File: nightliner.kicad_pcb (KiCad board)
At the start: 2 copper layers, 154.9 x 116.1 mm, 92 parts, among them J1 TYPE-C-31-M-12, J2 Battery, SW1 pinky_top, SW10 inner_home, SW11 pinky_bottom, SW12 ring_bottom, SW13 middle_bottom, SW14 index_bottom, SW15 inner_bottom, SW16 outer_top, SW17 outer_home, SW18 near_thumb, SW19 home_thumb, SW2 ring_top, SW20 far_thumb, SW21 ON_OFF, SW22 RESET, SW3 middle_top, SW4 index_top, SW5 inner_top, SW6 pinky_home, SW7 ring_home, SW8 middle_home, SW9 index_home, U1 holyiot-18010, U2 TVS2200DRV, U3 USBLC6-2SC6, U4 BQ24075RGT, U5 XC6220B331MR

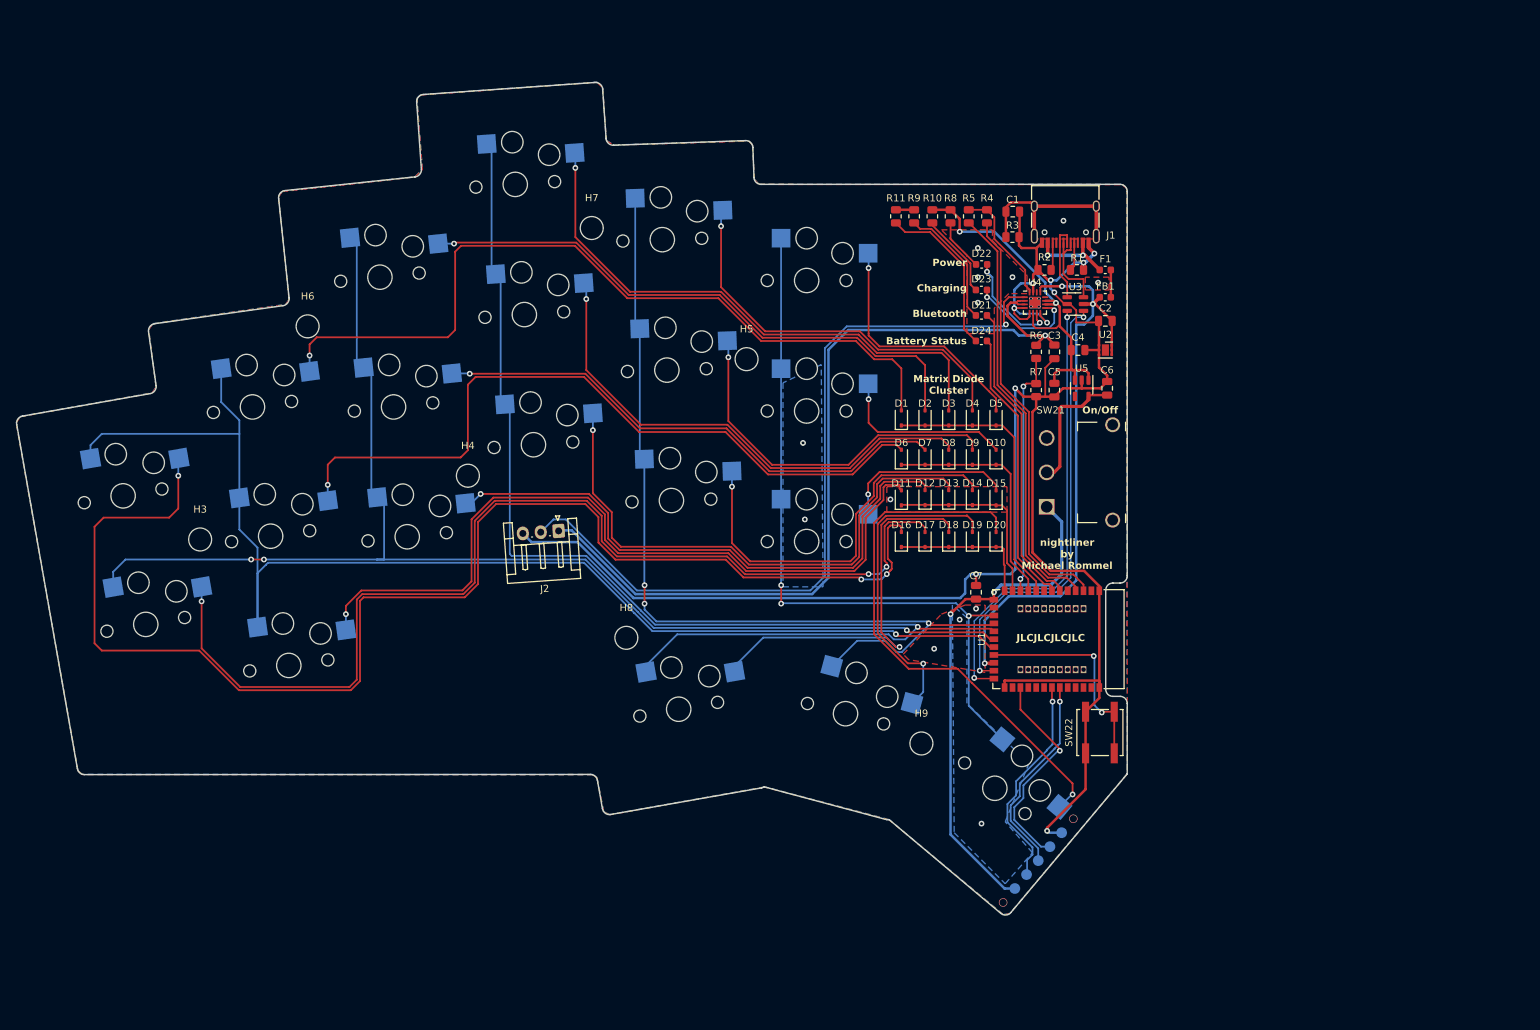
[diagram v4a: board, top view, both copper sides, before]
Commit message: feat: change connector and on/off switch, re-layout
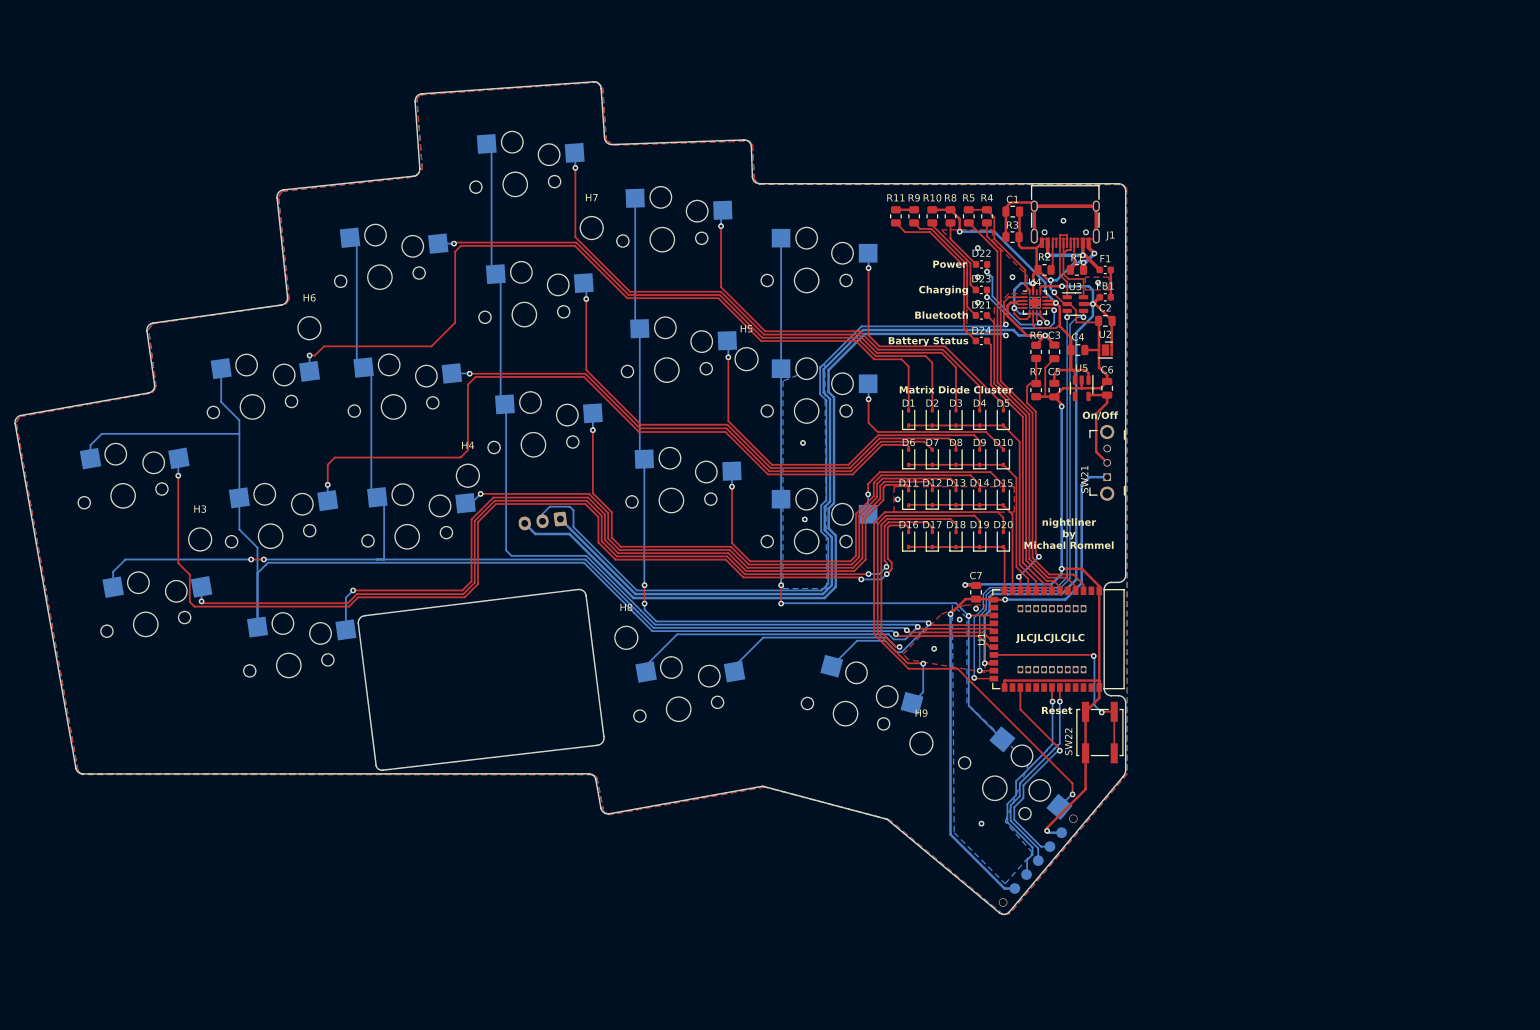
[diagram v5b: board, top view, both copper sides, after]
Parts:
- J2: footprint Connector_JST:JST_EH_S3B-EH_1x03_P2.50mm_Horizontal -> Connector_JST:JST_XH_S3B-XH-A-1_1x03_P2.50mm_Horizontal; moved to B.Cu
- SW21: footprint miro_keyboard:SW_XKB_SS-12D11_SPDT_Angled -> miro_keyboard:SW_ROCPU_SK-12D07-5_SPDT_Angled
- moved SW21 9.40 mm to (170.9, 78.4)
- moved J2 1.67 mm to (94.7, 84.3), turned to -173 degrees
- moved D13 1.02 mm to (149.9, 81.3)
- moved D14 1.02 mm to (153.2, 81.3)
- moved D18 1.02 mm to (149.9, 87.1)
- moved D19 1.02 mm to (153.2, 87.1)
- moved D3 1.02 mm to (149.9, 70.2)
- moved D4 1.02 mm to (153.2, 70.2)
- moved D8 1.02 mm to (149.9, 75.7)
- moved D9 1.02 mm to (153.2, 75.7)
- moved D1 1.02 mm to (143.3, 70.2)
- moved D10 1.02 mm to (156.5, 75.7)
- moved D11 1.02 mm to (143.3, 81.3)
- moved D12 1.02 mm to (146.6, 81.3)
- moved D15 1.02 mm to (156.5, 81.3)
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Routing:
- net Net-(D16-A): track 188.1 -> 146.7 mm
- net Net-(D17-A): track 148.0 -> 129.0 mm
- net GND: track 281.4 -> 296.3 mm, vias 23 -> 25
- net VDD: track 71.5 -> 80.7 mm
- net Net-(SW21-B): track 18.1 -> 13.4 mm
- net /BAT_TEMP: track 110.1 -> 113.9 mm
- net Net-(D11-A): track 108.5 -> 110.2 mm
- net D+: track 63.2 -> 64.8 mm
- net D-: track 63.1 -> 64.5 mm
- net VSENSE: track 34.1 -> 35.4 mm
- net Net-(D6-A): track 103.1 -> 104.3 mm
- net Net-(D2-A): track 81.3 -> 82.5 mm
- net Net-(D13-A): track 77.6 -> 78.6 mm
- net Net-(D9-A): track 51.1 -> 52.1 mm
- net Net-(D8-A): track 71.2 -> 72.2 mm
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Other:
- outline, holes or cut-outs redrawn
- board text added: "LiPo Battery (30mm x 20mm)"
- board text added: "Reset"

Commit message: fix: footprint for prog header, mounting holes, drc check
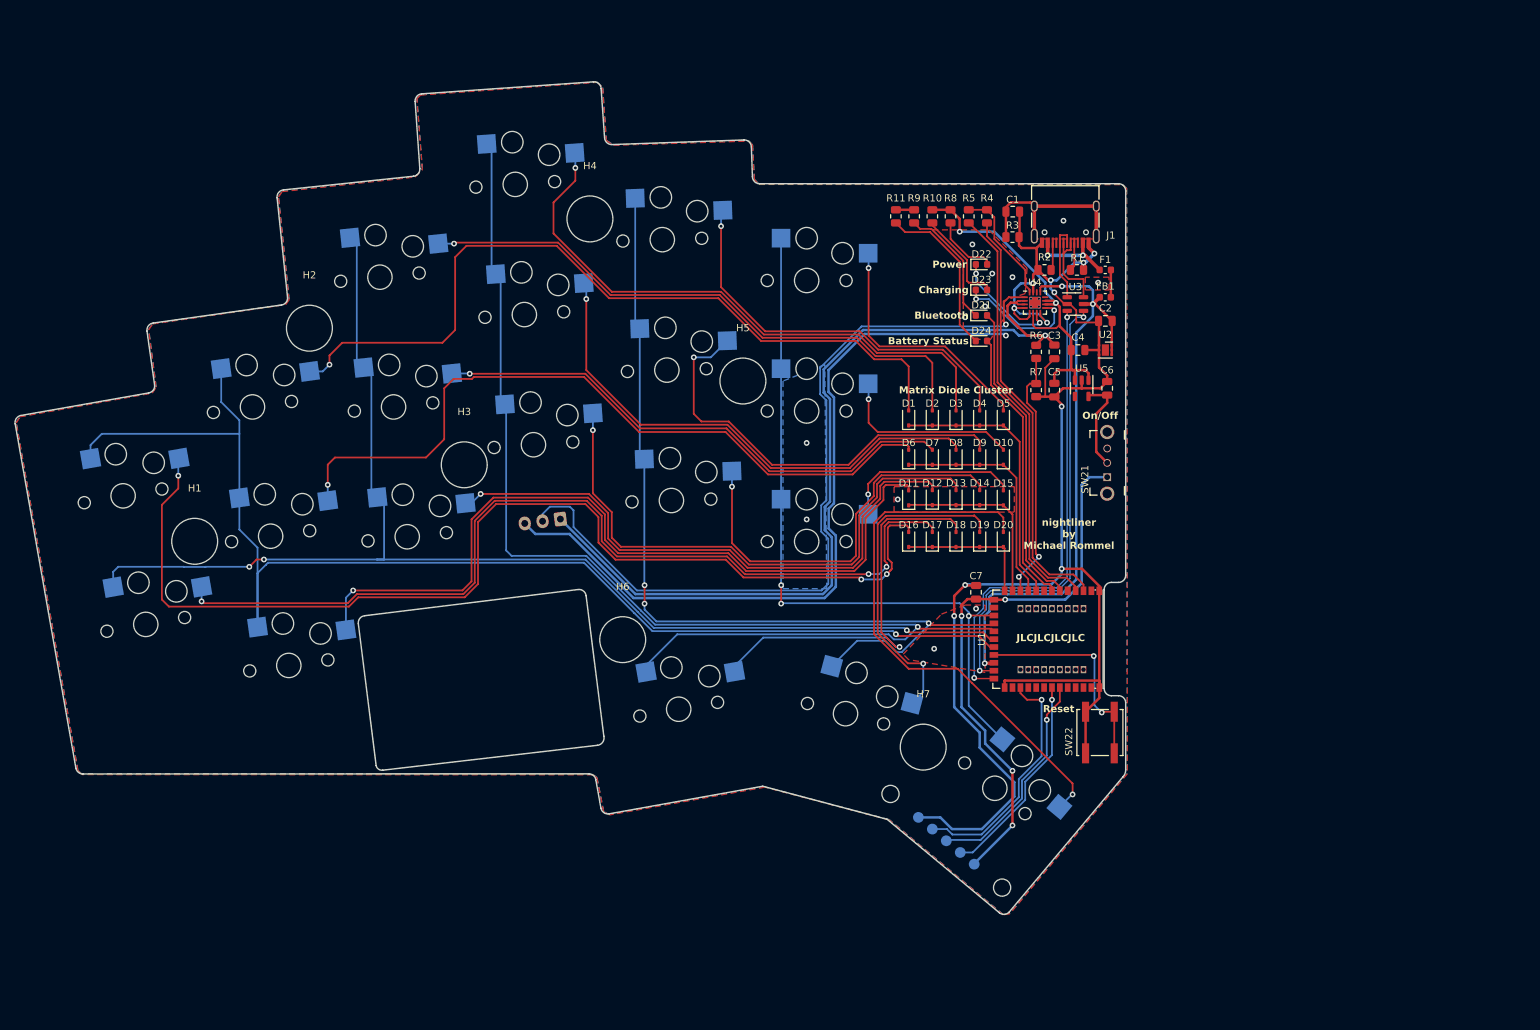
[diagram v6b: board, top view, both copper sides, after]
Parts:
- removed the H1 at (166.2, 126.1)
- removed the H2 at (156.4, 137.7)
- removed TP1, TP2, TP3, TP4, TP5: TestPoint, TestPoint:TestPoint_Pad_D1.5mm
- removed kibuzzard-653A69A4: G***, kibuzzard-653A69A4
- removed kibuzzard-653A69BD: G***, kibuzzard-653A69BD
- removed kibuzzard-653A69C5: G***, kibuzzard-653A69C5
- removed kibuzzard-653A69CD: G***, kibuzzard-653A69CD
- removed kibuzzard-653A69D7: G***, kibuzzard-653A69D7
- added P1: ISP_Prog, miro_keyboard:ISP_Programming_Pads, B.Cu at (156.3, 135.7)
- D21, D22, D23, D24: footprint Capacitor_SMD:C_0603_1608Metric -> LED_SMD:LED_0603_1608Metric
- F1: footprint Capacitor_SMD:C_0603_1608Metric -> Fuse:Fuse_0603_1608Metric
- H1: renamed from H3; footprint MountingHole:MountingHole_3.2mm_M3 -> MountingHole:MountingHole_6.4mm_M6
- H2: renamed from H6; footprint MountingHole:MountingHole_3.2mm_M3 -> MountingHole:MountingHole_6.4mm_M6
- H3: renamed from H4; footprint MountingHole:MountingHole_3.2mm_M3 -> MountingHole:MountingHole_6.4mm_M6
- H4: renamed from H7; footprint MountingHole:MountingHole_3.2mm_M3 -> MountingHole:MountingHole_6.4mm_M6
- H5: footprint MountingHole:MountingHole_3.2mm_M3 -> MountingHole:MountingHole_6.4mm_M6
- H6: renamed from H8; footprint MountingHole:MountingHole_3.2mm_M3 -> MountingHole:MountingHole_6.4mm_M6
- H7: renamed from H9; footprint MountingHole:MountingHole_3.2mm_M3 -> MountingHole:MountingHole_6.4mm_M6
- U1: footprint kleeb_mcu:holyiot-18010 -> miro_keyboard:holyiot-18010
- moved H5 3.09 mm to (120.1, 65.0)
- moved H3 1.61 mm to (81.3, 76.7)
- moved H4 1.30 mm to (98.8, 42.4)
- moved H1 0.80 mm to (43.7, 87.4)
- moved H7 0.57 mm to (145.3, 116.1)
- moved H6 0.57 mm to (103.4, 101.1)
- turned D22 to 0 degrees
- turned D23 to 0 degrees
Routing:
- net GND: track 296.3 -> 330.8 mm, vias 25 -> 24
- net Net-(D9-A): track 52.1 -> 59.6 mm
- net Net-(D3-A): track 78.4 -> 82.4 mm
- net Net-(D16-A): track 146.7 -> 150.7 mm
- net VDD: track 80.7 -> 77.1 mm, vias 2 -> 4
- net SWO: track 30.0 -> 33.6 mm
- net SWDIO: track 28.6 -> 30.7 mm
- net Net-(D22-A): track 7.27 -> 9.14 mm
- net Net-(D23-A): track 11.9 -> 13.7 mm
- net Net-(D23-K): track 15.6 -> 17.3 mm
- net SWCLK: track 30.5 -> 29.3 mm
- net Net-(D6-A): track 104.3 -> 103.1 mm
- net Net-(D22-K): track 14.7 -> 15.4 mm
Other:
- board text added: "GND"
- board text added: "VBAT"

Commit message: feat: move all outlines to KiCAD, update footprints
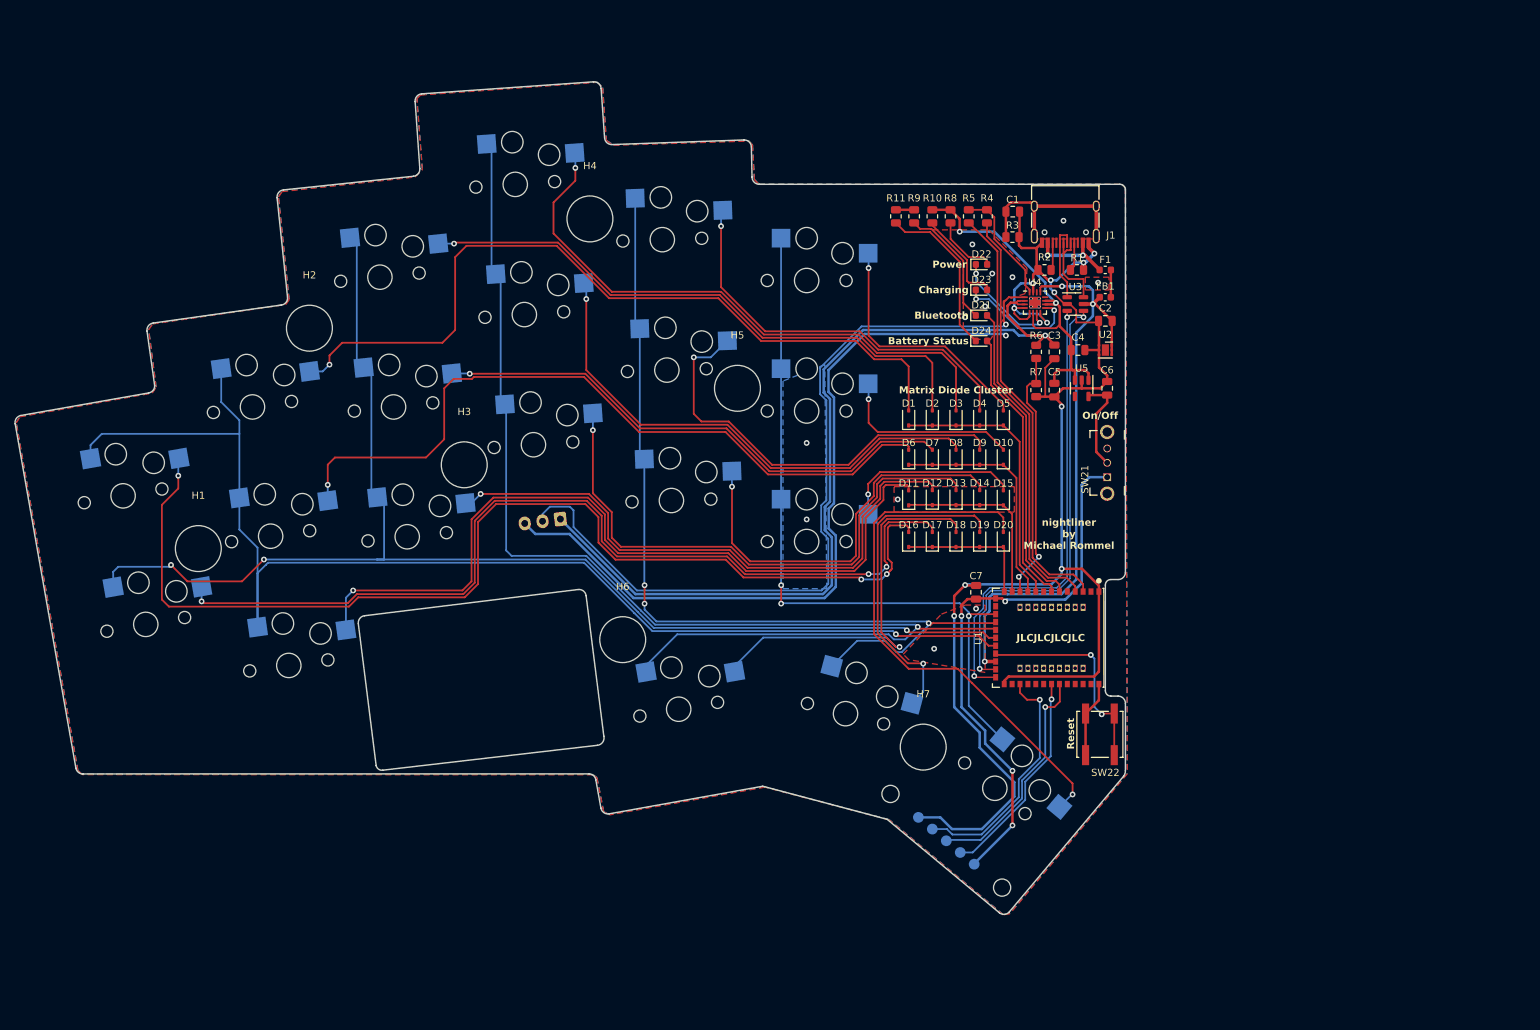
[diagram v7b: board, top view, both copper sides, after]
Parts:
- SW1, SW10, SW11, SW12, SW13, SW14, SW15, SW16, SW17, SW18, SW19, SW2, SW20, SW3, SW4, SW5, SW6, SW7, SW8, SW9: footprint kleeb_choc:pg1350-H -> miro_keyboard:Kailh_Choc_CPG135001D02_Hotswap
- U1: footprint miro_keyboard:holyiot-18010 -> miro_keyboard:HOLYIOT-18010-UndersidePins-SMD
- moved H5 1.27 mm to (119.4, 66.0)
- moved H1 1.14 mm to (44.2, 88.4)
- moved SW22 0.25 mm to (169.9, 114.3)
- moved U1 0.19 mm to (164.1, 100.8)
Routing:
- net GND: track 330.8 -> 327.9 mm
- net COL1: track 178.1 -> 180.2 mm
- net SWDIO: track 30.7 -> 31.4 mm
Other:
- board size 154.9 x 116.1 mm -> 154.8 x 116.1 mm
